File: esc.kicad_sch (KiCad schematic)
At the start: 71 parts, among them J8 Conn_01x04, Q10 NMOS, Q5 NMOS, Q6 NMOS, Q7 NMOS, Q8 NMOS, Q9 NMOS, U15 STM32G071K8U6, U16 DRV8328ARUYR, U7 INA190A3IDCKR

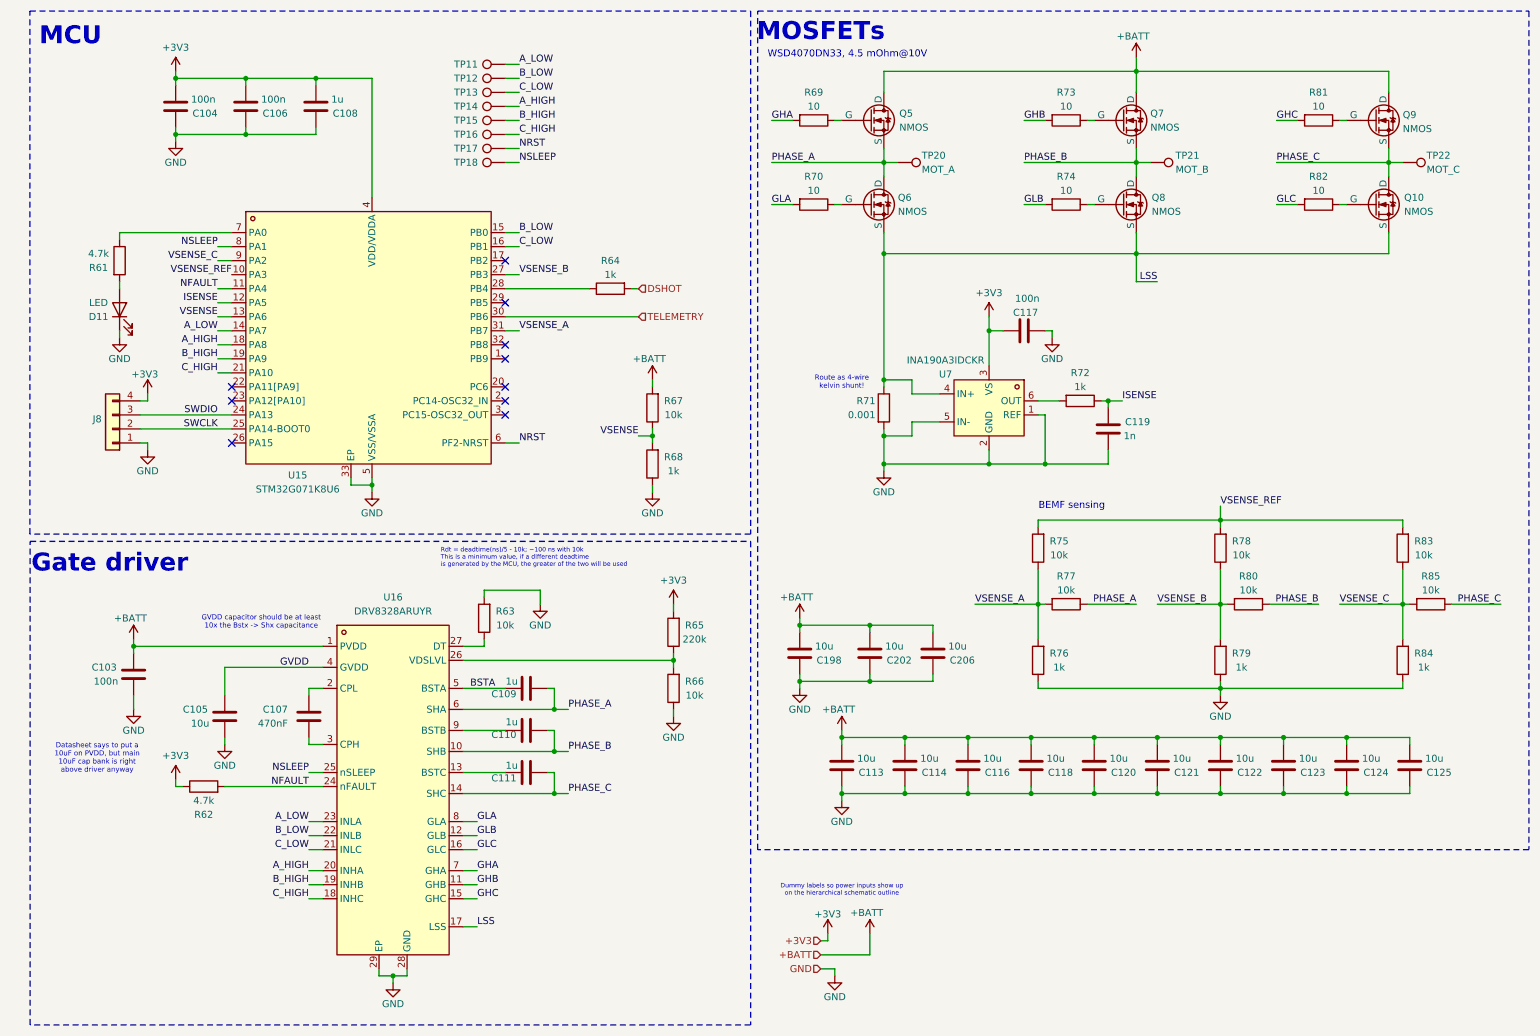
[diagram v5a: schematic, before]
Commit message: Minimize passive footprints again and switch ESC mcu to smaller footprint
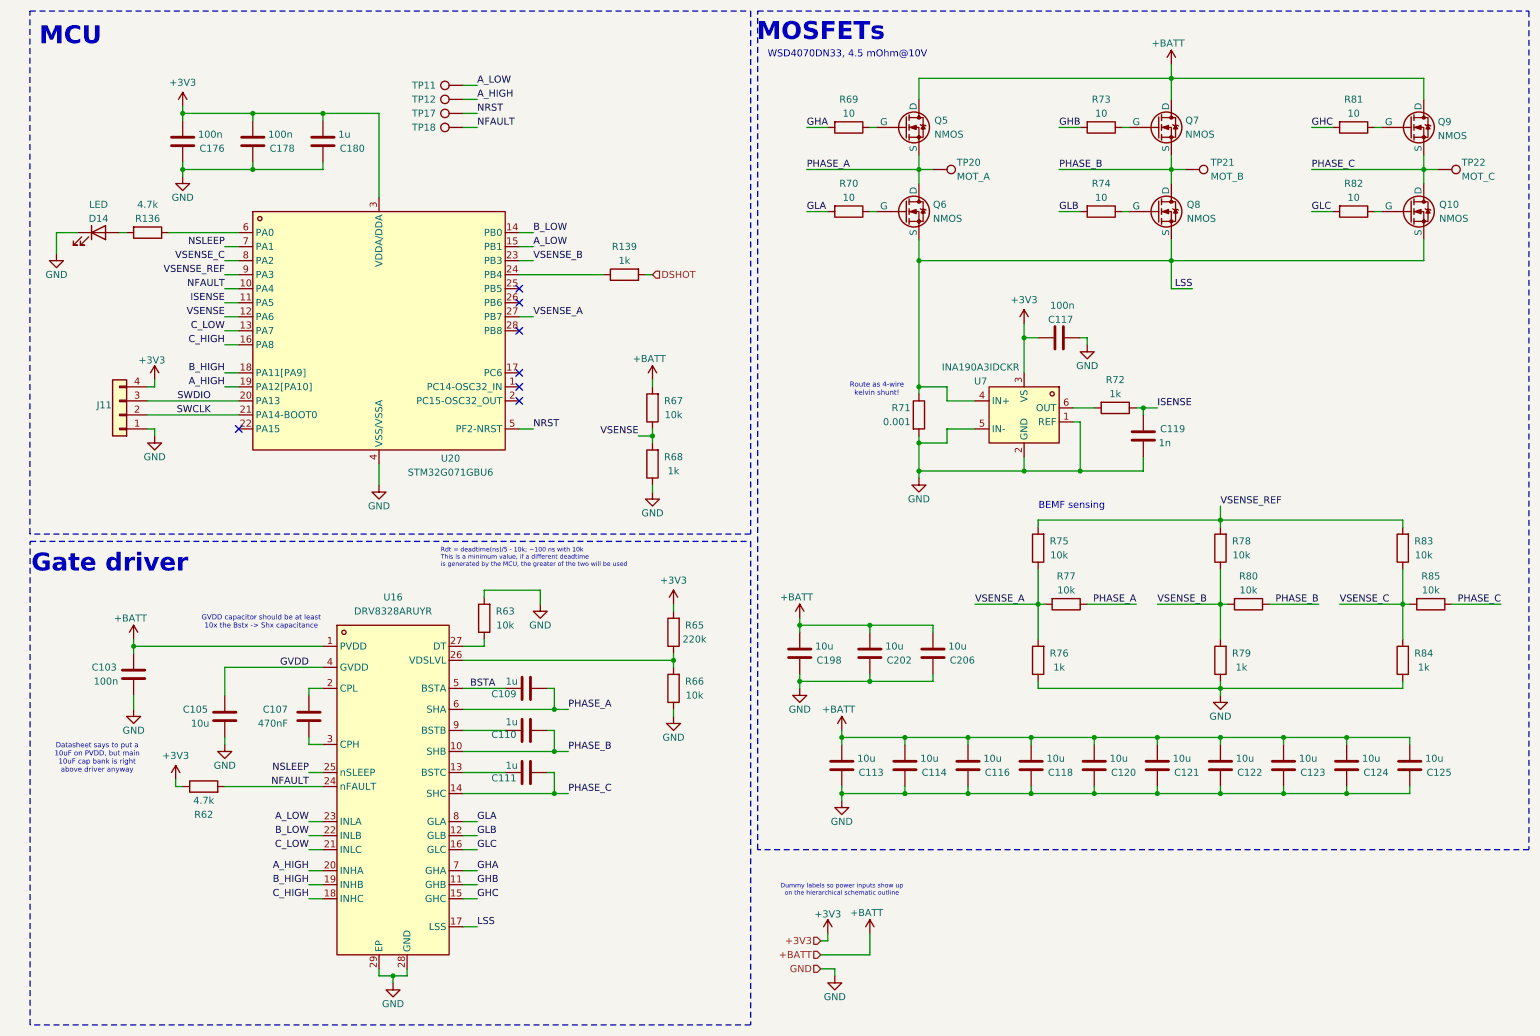
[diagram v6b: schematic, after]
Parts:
- removed C104, C106: 100n, Capacitor_SMD:C_0402_1005Metric, symbol Device:C
- removed C108: 1u, Capacitor_SMD:C_0603_1608Metric, symbol Device:C
- removed D11: LED, LED_SMD:LED_0402_1005Metric, symbol Device:LED
- removed J8: Conn_01x04, easyeda2kicad:Connector_Pad_1.27mm_1x04, symbol Connector_Generic:Conn_01x04
- removed R61: 4.7k, Resistor_SMD:R_0201_0603Metric, symbol Device:R
- removed R64: 1k, Resistor_SMD:R_0201_0603Metric, symbol Device:R
- removed TP13, TP14, TP15, TP16: TestPoint, easyeda2kicad:TestPoint_Pad_D1.0mm_No_Courtyard, symbol Connector:TestPoint
- removed U15: STM32G071K8U6, easyeda2kicad:UFQFPN-32_L5.0-W5.0-P0.50-TL-EP3.5, symbol easyeda2kicad:STM32G071K8U6
- added C176, C178: 100n, Capacitor_SMD:C_0201_0603Metric, symbol Device:C
- added C180: 1u, Capacitor_SMD:C_0402_1005Metric, symbol Device:C
- added D14: LED, LED_SMD:LED_0402_1005Metric, symbol Device:LED
- added J11: Conn_01x04, easyeda2kicad:Connector_Pad_1.27mm_1x04, symbol Connector_Generic:Conn_01x04
- added R136: 4.7k, Resistor_SMD:R_0201_0603Metric, symbol Device:R
- added R139: 1k, Resistor_SMD:R_0201_0603Metric, symbol Device:R
- added U20: STM32G071GBU6, easyeda2kicad:UFQFPN-28_L4.0-W4.0-P0.50-BL, symbol easyeda2kicad:STM32G071GBU6
- C117: footprint Capacitor_SMD:C_0402_1005Metric -> Capacitor_SMD:C_0201_0603Metric
- R72: footprint Resistor_SMD:R_0402_1005Metric -> Resistor_SMD:R_0201_0603Metric
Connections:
- net +3V3: now also C176.2, C178.2, C180.2, J11.4 (Pin_4), U20.3 (VDDA/DDA)
- net A_HIGH: now also TP12.1, U20.19 (PA12[PA10])
- net A_LOW: now also U20.15 (PB1)
- net B_HIGH: now also U20.18 (PA11[PA9])
- net B_LOW: now also U20.14 (PB0); no longer TP12.1
- net C_HIGH: now also U20.16 (PA8)
- net C_LOW: now also U20.13 (PA7)
- net DSHOT: now also R139.2
- net GND: now also C176.1, C178.1, C180.1, D14.1 (K), J11.1 (Pin_1), U20.4 (VSS/VSSA)
- net ISENSE: now also U20.11 (PA5)
- net NFAULT: now also TP18.1, U20.10 (PA4)
- net NRST: now also U20.5 (PF2-NRST)
- net NSLEEP: now also U20.7 (PA1); no longer TP18.1
- net SWCLK: now also J11.2 (Pin_2), U20.21 (PA14-BOOT0)
- net SWDIO: now also J11.3 (Pin_3), U20.20 (PA13)
- net VSENSE: now also U20.12 (PA6)
- net VSENSE_A: now also U20.27 (PB7)
- net VSENSE_B: now also U20.23 (PB3)
- net VSENSE_C: now also U20.8 (PA2)
- net VSENSE_REF: now also U20.9 (PA3)
- new net: R139.1, U20.24 (PB4)
- new net: D14.2 (A), R136.2
- new net: R136.1, U20.6 (PA0)
- no-connect marks 10 -> 7
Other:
- moved on the sheet: C117, C119, Q10, Q5, Q6, Q7, Q8, Q9, R69, R70, R71, R72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

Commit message: ESC routing experiments
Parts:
- C107: footprint Capacitor_SMD:C_0603_1608Metric -> Capacitor_SMD:C_0402_1005Metric
- C119: footprint Capacitor_SMD:C_0402_1005Metric -> Capacitor_SMD:C_0201_0603Metric
- R71: footprint Resistor_SMD:R_2512_6332Metric -> Resistor_SMD:R_1206_3216Metric
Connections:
- net A_HIGH: now also U20.16 (PA8); no longer U20.19 (PA12[PA10])
- net A_LOW: now also U20.13 (PA7); no longer U20.15 (PB1)
- net C_HIGH: now also U20.19 (PA12[PA10]); no longer U20.16 (PA8)
- net C_LOW: now also U20.15 (PB1); no longer U20.13 (PA7)
- net at U20.28 (PB8): now also R136.1
- net at U20.6 (PA0): no longer R136.1
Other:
- moved on the sheet: R67, R68, TP11, TP12, TP17, TP18

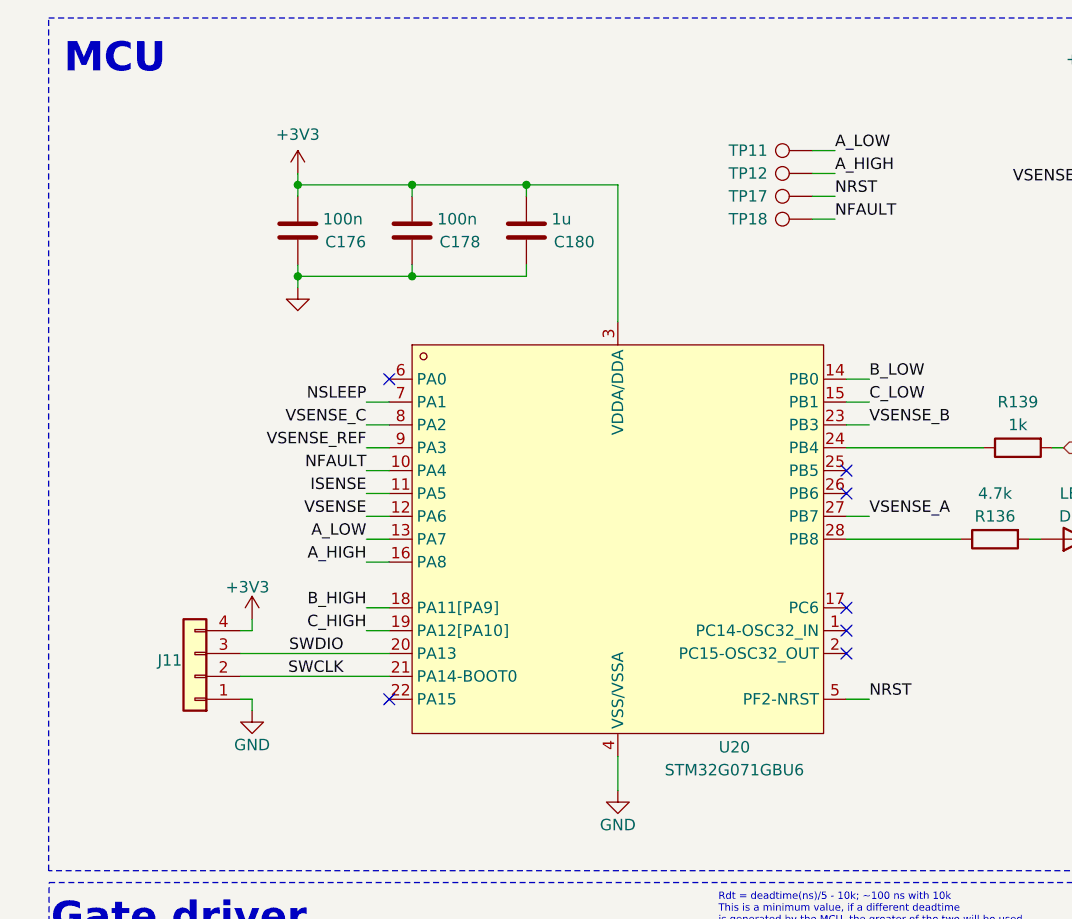
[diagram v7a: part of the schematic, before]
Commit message: Moar ESC routing
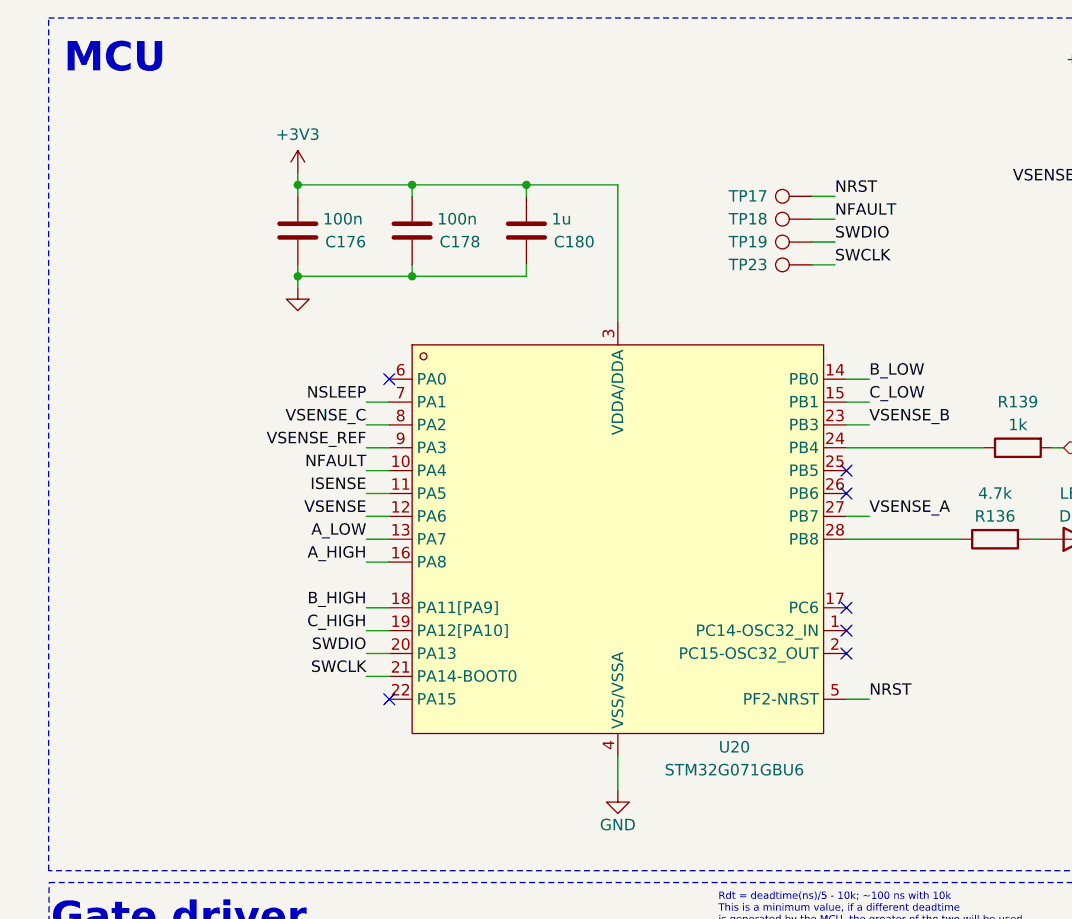
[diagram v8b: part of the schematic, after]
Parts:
- removed J11: Conn_01x04, easyeda2kicad:Connector_Pad_1.27mm_1x04, symbol Connector_Generic:Conn_01x04
- removed TP11, TP12: TestPoint, easyeda2kicad:TestPoint_Pad_D1.0mm_No_Courtyard, symbol Connector:TestPoint
- added TP19, TP23: TestPoint, easyeda2kicad:TestPoint_Pad_D1.0mm_No_Courtyard, symbol Connector:TestPoint
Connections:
- net SWCLK: now also TP23.1
- net SWDIO: now also TP19.1
